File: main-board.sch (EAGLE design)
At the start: 56 parts, among them IC1 MEGA328-PB, IC2 MCP73831, IC3 LE33, Q1 3,6864 MHz, Q4 TSM2302CX, T1 IRF7306

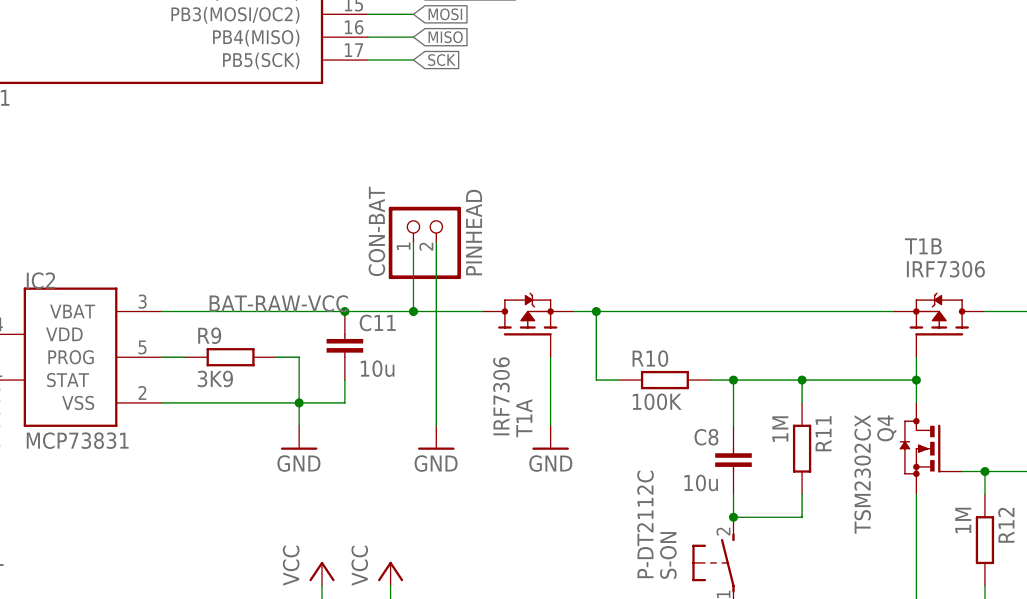
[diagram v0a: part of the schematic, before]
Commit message: Protect charging circuit against polarity change too.
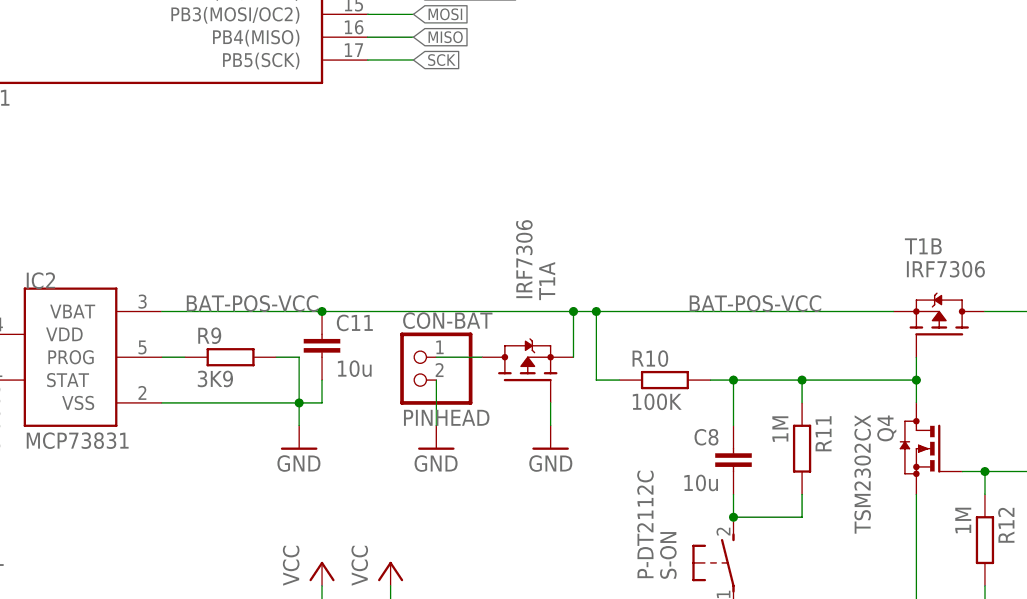
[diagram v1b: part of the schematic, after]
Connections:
- net BAT-POS-VCC: now also C11.1, IC2.VBAT
- net BAT-RAW-VCC: no longer C11.1, IC2.VBAT
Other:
- moved on the sheet: C11, CON-BAT, T1A
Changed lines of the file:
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@@
 <attribute name="VALUE" x="30.48" y="53.34" size="1.778" layer="96"/>
 </instance>
-<instance part="CON-BAT" gate="G$1" x="99.06" y="81.28" smashed="yes" rot="R90">
-<attribute name="NAME" x="93.345" y="74.93" size="1.778" layer="95" rot="R90"/>
-<attribute name="VALUE" x="104.14" y="74.93" size="1.778" layer="96" rot="R90"/>
+<instance part="CON-BAT" gate="G$1" x="96.52" y="63.5" smashed="yes" rot="MR0">
+<attribute name="NAME" x="95.25" y="69.215" size="1.778" layer="95"/>
+<attribute name="VALUE" x="95.25" y="58.42" size="1.778" layer="96"/>
 </instance>
 <instance part="GND11" gate="1" x="99.06" y="55.88" smashed="yes">
@@
 <attribute name="VALUE" x="167.64" y="73.66" size="1.778" layer="96" rot="R90"/>
 </instance>
-<instance part="C11" gate="G$1" x="88.9" y="68.58" smashed="yes">
-<attribute name="NAME" x="90.424" y="68.961" size="1.778" layer="95"/>
-<attribute name="VALUE" x="90.424" y="63.881" size="1.778" layer="96"/>
+<instance part="C11" gate="G$1" x="86.36" y="68.58" smashed="yes">
+<attribute name="NAME" x="87.884" y="68.961" size="1.778" layer="95"/>
+<attribute name="VALUE" x="87.884" y="63.881" size="1.778" layer="96"/>
 </instance>
 <instance part="C5" gate="G$1" x="33.02" y="66.04" smashed="yes">
@@
 <attribute name="VALUE" x="154.94" y="114.3" size="1.778" layer="96"/>
 </instance>
-<instance part="T1" gate="A" x="109.22" y="68.58" smashed="yes" rot="MR90">
-<attribute name="VALUE" x="105.41" y="57.15" size="1.778" layer="96" rot="MR90"/>
-<attribute name="NAME" x="107.95" y="57.15" size="1.778" layer="95" rot="MR90"/>
+<instance part="T1" gate="A" x="109.22" y="63.5" smashed="yes" rot="MR90">
+<attribute name="VALUE" x="107.95" y="72.39" size="1.778" layer="96" rot="MR90"/>
+<attribute name="NAME" x="110.49" y="72.39" size="1.778" layer="95" rot="MR90"/>
 </instance>
 <instance part="T1" gate="B" x="154.94" y="68.58" smashed="yes" rot="R90">
@@
 <wire x1="83.82" y1="66.04" x2="83.82" y2="60.96" width="0.1524" layer="91"/>
 <junction x="83.82" y="60.96"/>
-<wire x1="83.82" y1="60.96" x2="88.9" y2="60.96" width="0.1524" layer="91"/>
-<wire x1="88.9" y1="60.96" x2="88.9" y2="63.5" width="0.1524" layer="91"/>
+<wire x1="83.82" y1="60.96" x2="86.36" y2="60.96" width="0.1524" layer="91"/>
+<wire x1="86.36" y1="60.96" x2="86.36" y2="63.5" width="0.1524" layer="91"/>
 <pinref part="C11" gate="G$1" pin="2"/>
 </segment>
@@
 <segment>
 <pinref part="CON-BAT" gate="G$1" pin="2"/>
-<wire x1="99.06" y1="58.42" x2="99.06" y2="78.74" width="0.1524" layer="91"/>
+<wire x1="99.06" y1="58.42" x2="99.06" y2="63.5" width="0.1524" layer="91"/>
 <pinref part="GND11" gate="1" pin="GND"/>
 </segment>
@@
 <pinref part="GND18" gate="1" pin="GND"/>
 <pinref part="T1" gate="A" pin="G"/>
-<wire x1="111.76" y1="58.42" x2="111.76" y2="66.04" width="0.1524" layer="91"/>
+<wire x1="111.76" y1="58.42" x2="111.76" y2="60.96" width="0.1524" layer="91"/>
 </segment>
 <segment>
@@
 </segment>
 </net>
-<net name="BAT-RAW-VCC" class="1">
-<segment>
-<pinref part="CON-BAT" gate="G$1" pin="1"/>
-<wire x1="96.52" y1="71.12" x2="96.52" y2="78.74" width="0.1524" layer="91"/>
-<pinref part="IC2" gate="G$1" pin="VBAT"/>
-<wire x1="68.58" y1="71.12" x2="88.9" y2="71.12" width="0.1524" layer="91"/>
-<pinref part="C11" gate="G$1" pin="1"/>
-<wire x1="88.9" y1="71.12" x2="96.52" y2="71.12" width="0.1524" layer="91"/>
-<junction x="88.9" y="71.12"/>
-<label x="73.66" y="71.12" size="1.778" layer="95"/>
-<pinref part="T1" gate="A" pin="D"/>
-<wire x1="104.14" y1="71.12" x2="96.52" y2="71.12" width="0.1524" layer="91"/>
-<junction x="96.52" y="71.12"/>
-</segment>
-</net>
 <net name="LED-RED" class="0">
 <segment>
@@
 <wire x1="116.84" y1="71.12" x2="149.86" y2="71.12" width="0.1524" layer="91"/>
 <pinref part="T1" gate="B" pin="S"/>
-<pinref part="T1" gate="A" pin="S"/>
+<pinref part="IC2" gate="G$1" pin="VBAT"/>
+<wire x1="68.58" y1="71.12" x2="86.36" y2="71.12" width="0.1524" layer="91"/>
+<pinref part="C11" gate="G$1" pin="1"/>
+<junction x="86.36" y="71.12"/>
+<label x="127" y="71.12" size="1.778" layer="95"/>
 <wire x1="116.84" y1="71.12" x2="114.3" y2="71.12" width="0.1524" layer="91"/>
 <junction x="116.84" y="71.12"/>
+<pinref part="T1" gate="A" pin="S"/>
+<wire x1="114.3" y1="71.12" x2="86.36" y2="71.12" width="0.1524" layer="91"/>
+<wire x1="114.3" y1="66.04" x2="114.3" y2="71.12" width="0.1524" layer="91"/>
+<junction x="114.3" y="71.12"/>
+<label x="71.12" y="71.12" size="1.778" layer="95"/>
 </segment>
 </net>
@@
 </segment>
 </net>
+<net name="BAT-RAW-VCC" class="1">
+<segment>
+<pinref part="T1" gate="A" pin="D"/>
+<pinref part="CON-BAT" gate="G$1" pin="1"/>
+<wire x1="104.14" y1="66.04" x2="99.06" y2="66.04" width="0.1524" layer="91"/>
+</segment>
+</net>
